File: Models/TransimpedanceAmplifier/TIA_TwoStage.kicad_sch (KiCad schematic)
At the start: 8 parts

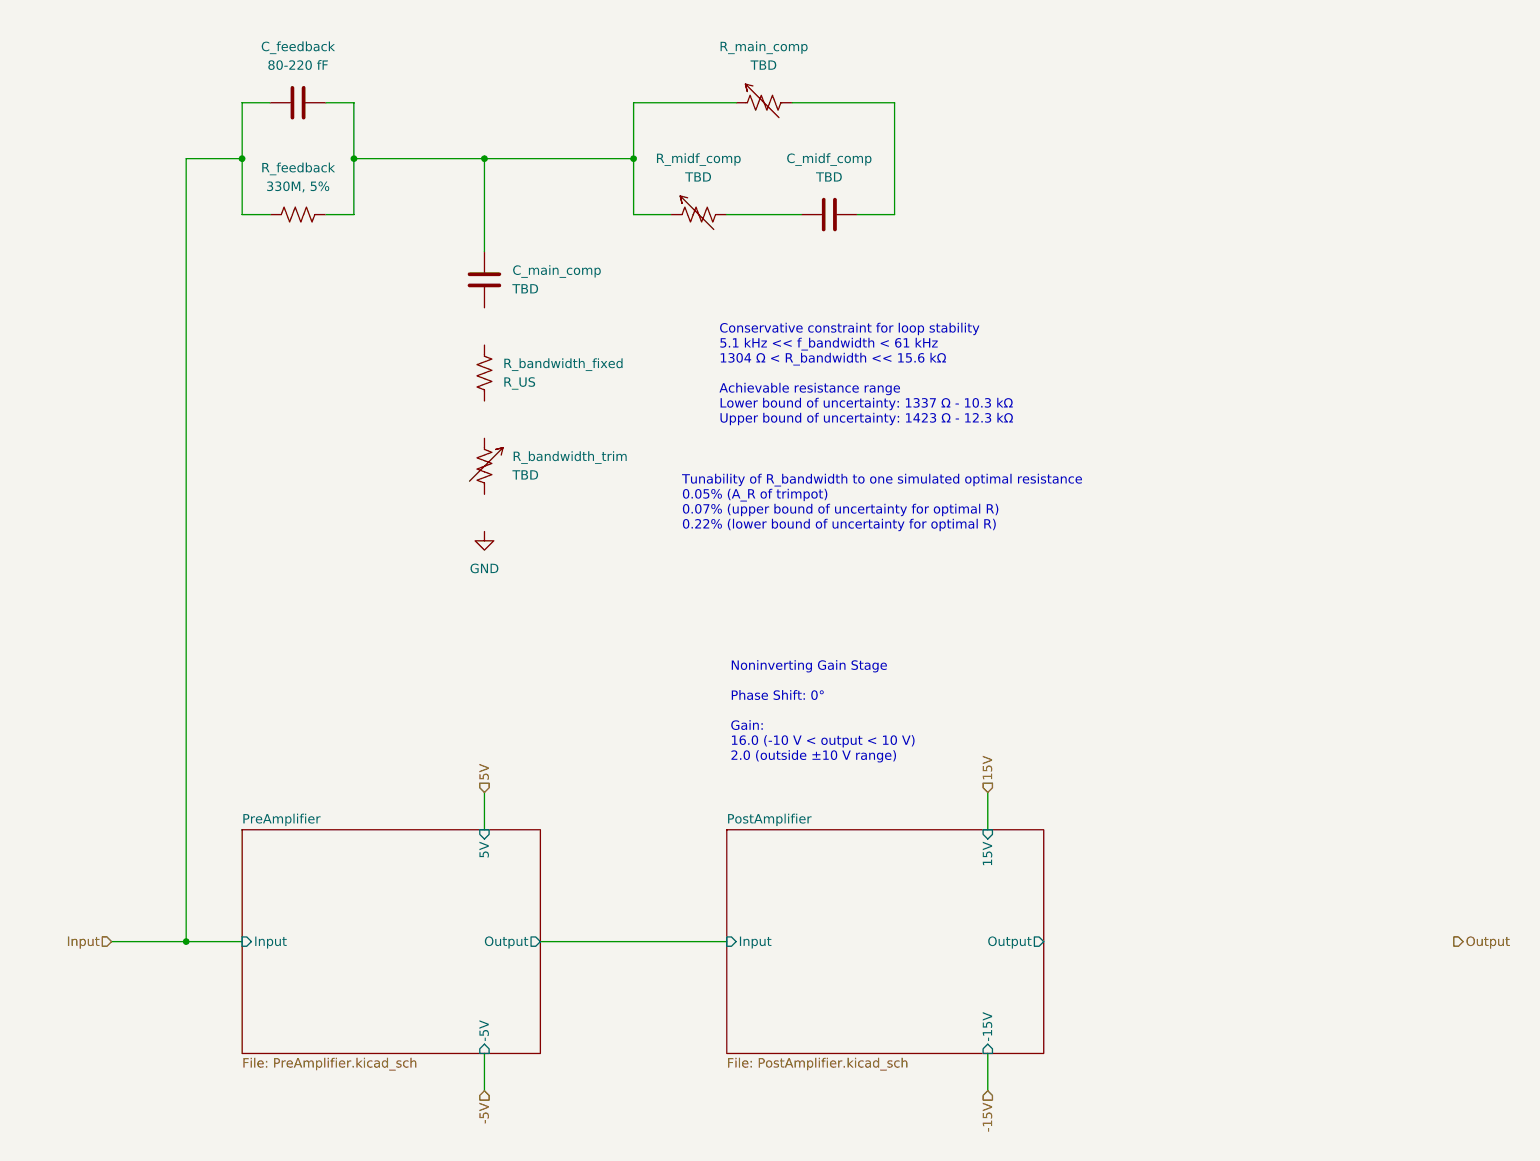
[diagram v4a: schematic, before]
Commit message: Figured out the specific part values for the pole-zero compensation network
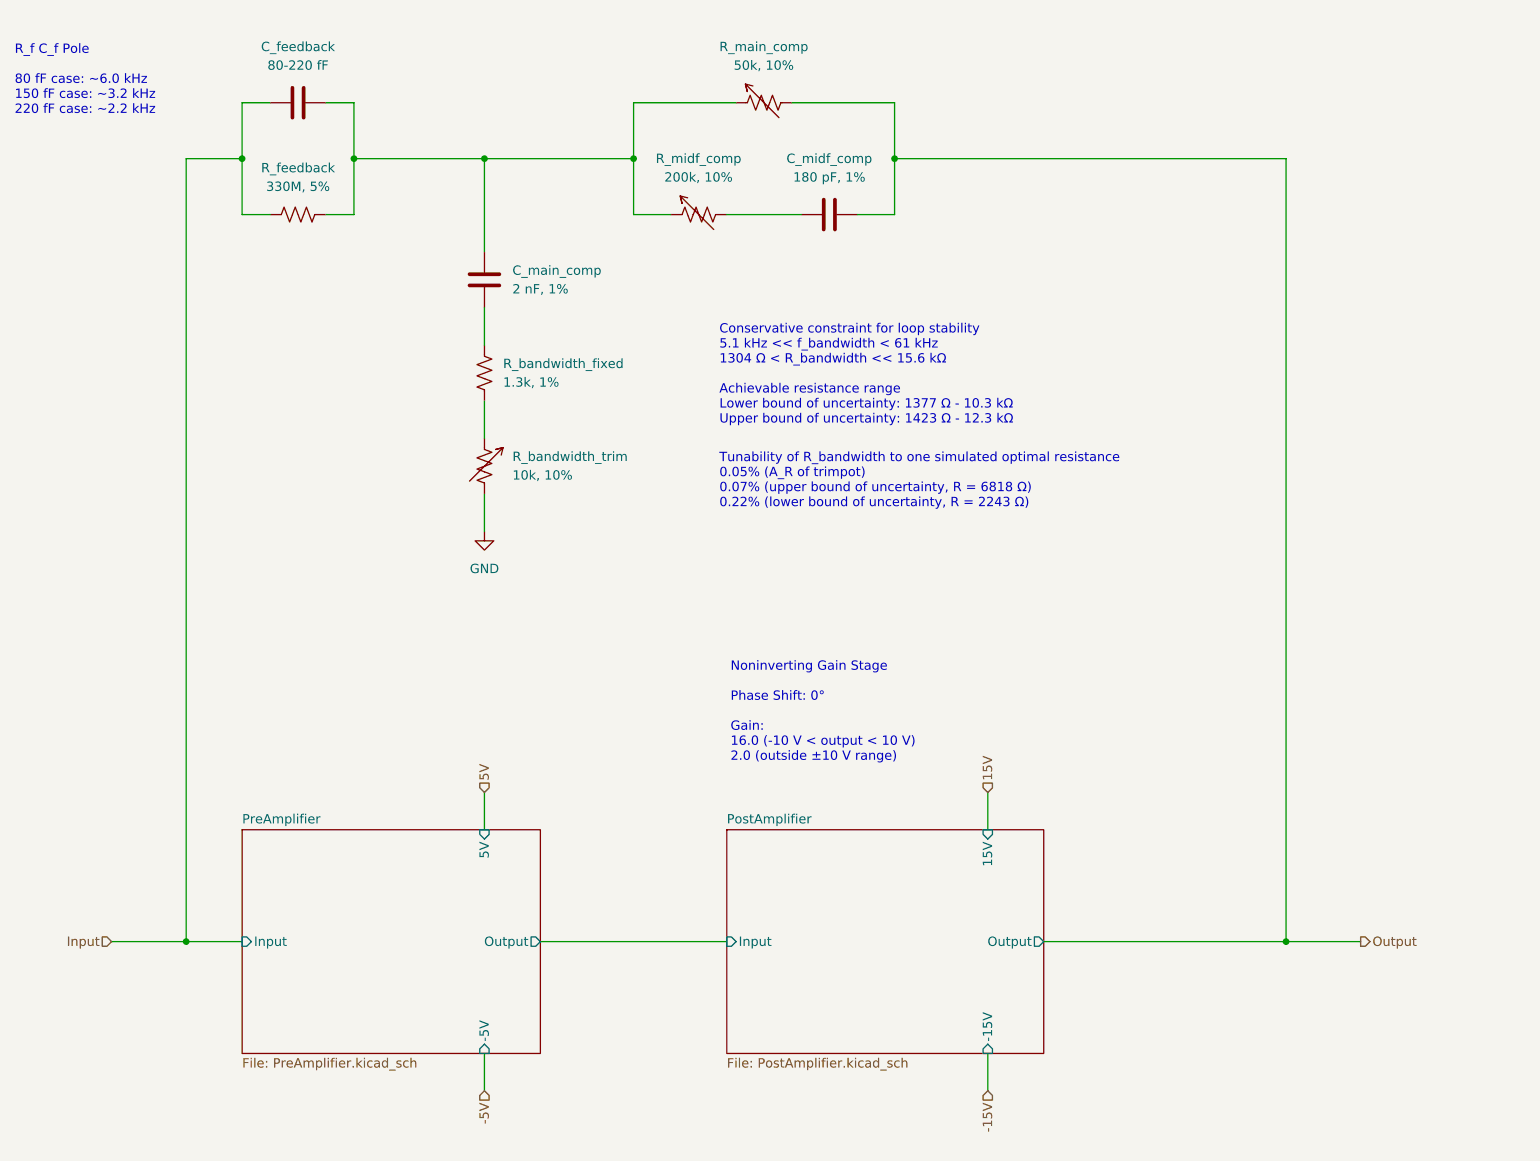
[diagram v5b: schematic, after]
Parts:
- C_main_comp: value TBD -> 2 nF, 1%; Purchase Link (none) -> https://www.digikey.com/en/products/detail/murata-electroni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
- C_midf_comp: value TBD -> 180 pF, 1%; Purchase Link (none) -> https://www.digikey.com/en/products/detail/murata-electroni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
- R_bandwidth_fixed: value R_US -> 1.3k, 1%; Purchase Link (none) -> https://www.digikey.com/en/products/detail/vishay-dale/CRCW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
- R_bandwidth_trim: value TBD -> 10k, 10%
- R_main_comp: value TBD -> 50k, 10%
- R_midf_comp: value TBD -> 200k, 10%
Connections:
- net GND: now also R_bandwidth_trim.2
- net Output: now also C_midf_comp.2, R_main_comp.2
- net at C_main_comp.2: now also R_bandwidth_fixed.1
- net at R_bandwidth_fixed.2: now also R_bandwidth_trim.1
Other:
- note added: "Conservative constraint for loop stability 5.1 kHz << f_bandwidth < 61 kHz 1304 Ω < R_bandwidth << 15.6 kΩ Achievable resistance range Lower bound of uncertainty: 1377 Ω - 10.3 kΩ Upper bound of uncertainty: 1423 Ω - 12.3 kΩ"
- note added: "R_f C_f Pole 80 fF case: ~6.0 kHz 150 fF case: ~3.2 kHz 220 fF case: ~2.2 kHz"
- note added: "Tunability of R_bandwidth to one simulated optimal resistance 0.05% (A_R of trimpot) 0.07% (upper bound of uncertainty, R = 6818 Ω) 0.22% (lower bound of uncertainty, R = 2243 Ω)"
- note removed: "Conservative constraint for loop stability 5.1 kHz << f_bandwidth < 61 kHz 1304 Ω < R_bandwidth << 15.6 kΩ Achievable resistance range Lower bound of uncertainty: 1337 Ω - 10.3 kΩ Upper bound of uncertainty: 1423 Ω - 12.3 kΩ"
- note removed: "Tunability of R_bandwidth to one simulated optimal resistance 0.05% (A_R of trimpot) 0.07% (upper bound of uncertainty for optimal R) 0.22% (lower bound of uncertainty for optimal R)"
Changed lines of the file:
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@@
 	(generator_version "9.0")
 	(paper "A4")
-	(text "Conservative constraint for loop stability\n5.1 kHz << f_bandwidth < 61 kHz\n1304 Ω < R_bandwidth << 15.6 kΩ\n\nAchievable resistance range\nLower bound of uncertainty: 1337 Ω - 10.3 kΩ\nUpper bound of uncertainty: 1423 Ω - 12.3 kΩ"
+	(text "Conservative constraint for loop stability\n5.1 kHz << f_bandwidth < 61 kHz\n1304 Ω < R_bandwidth << 15.6 kΩ\n\nAchievable resistance range\nLower bound of uncertainty: 1377 Ω - 10.3 kΩ\nUpper bound of uncertainty: 1423 Ω - 12.3 kΩ"
 		(exclude_from_sim no)
 		(at 125.984 63.246 0)
@@
 		)
 	)
-	(text "Tunability of R_bandwidth to one simulated optimal resistance\n0.05% (A_R of trimpot)\n0.07% (upper bound of uncertainty for optimal R)\n0.22% (lower bound of uncertainty for optimal R)"
-		(exclude_from_sim no)
-		(at 120.904 83.82 0)
+	(text "Tunability of R_bandwidth to one simulated optimal resistance\n0.05% (A_R of trimpot)\n0.07% (upper bound of uncertainty, R = 6818 Ω)\n0.22% (lower bound of uncertainty, R = 2243 Ω)"
+		(exclude_from_sim no)
+		(at 125.984 80.772 0)
+		(effects
+			(font
+				(size 1.27 1.27)
+			)
+			(justify left top)
+		)
+	)
+	(text "R_f C_f Pole\n\n80 fF case: ~6.0 kHz\n150 fF case: ~3.2 kHz\n220 fF case: ~2.2 kHz"
+		(exclude_from_sim no)
+		(at 29.972 25.146 0)
 		(effects
 			(font
@@
 	)
 	(junction
+		(at 149.86 40.64)
+		(diameter 0)
+		(color 0 0 0 0)
+	)
+	(junction
 		(at 60.96 40.64)
 		(diameter 0)
@@
 	)
 	(junction
+		(at 203.2 147.32)
+		(diameter 0)
+		(color 0 0 0 0)
+	)
+	(junction
 		(at 114.3 40.64)
 		(diameter 0)
@@
 	(wire
 		(pts
+			(xy 93.98 86.36) (xy 93.98 91.44)
+		)
+		(stroke
+			(width 0)
+			(type default)
+		)
+	)
+	(wire
+		(pts
 			(xy 76.2 40.64) (xy 93.98 40.64)
 		)
@@
 	(wire
 		(pts
+			(xy 149.86 40.64) (xy 203.2 40.64)
+		)
+		(stroke
+			(width 0)
+			(type default)
+		)
+	)
+	(wire
+		(pts
 			(xy 93.98 162.56) (xy 93.98 167.64)
 		)
@@
 	(wire
 		(pts
-			(xy 149.86 33.02) (xy 149.86 48.26)
+			(xy 170.18 147.32) (xy 203.2 147.32)
+		)
+		(stroke
+			(width 0)
+			(type default)
+		)
+	)
+	(wire
+		(pts
+			(xy 149.86 33.02) (xy 149.86 40.64)
 		)
 		(stroke
@@
 	(wire
 		(pts
+			(xy 203.2 147.32) (xy 213.36 147.32)
+		)
+		(stroke
+			(width 0)
+			(type default)
+		)
+	)
+	(wire
+		(pts
+			(xy 93.98 60.96) (xy 93.98 66.04)
+		)
+		(stroke
+			(width 0)
+			(type default)
+		)
+	)
+	(wire
+		(pts
 			(xy 53.34 147.32) (xy 60.96 147.32)
 		)
@@
 	(wire
 		(pts
+			(xy 149.86 40.64) (xy 149.86 48.26)
+		)
+		(stroke
+			(width 0)
+			(type default)
+		)
+	)
+	(wire
+		(pts
 			(xy 60.96 40.64) (xy 53.34 40.64)
+		)
+		(stroke
+			(width 0)
+			(type default)
+		)
+	)
+	(wire
+		(pts
+			(xy 203.2 40.64) (xy 203.2 147.32)
+		)
+		(stroke
+			(width 0)
+			(type default)
+		)
+	)
+	(wire
+		(pts
+			(xy 93.98 73.66) (xy 93.98 78.74)
 		)
 		(stroke
@@
 	(hierarchical_label "Output"
 		(shape output)
-		(at 226.06 147.32 0)
+		(at 213.36 147.32 0)
 		(effects
 			(font
@@
 			)
 		)
-		(property "Value" "TBD"
+		(property "Value" "2 nF, 1%"
 			(at 97.79 58.4199 0)
 			(effects
@@
 		)
 		(property "Description" "Unpolarized capacitor"
+			(at 93.98 57.15 0)
+			(effects
+				(font
+					(size 1.27 1.27)
+				)
+				(hide yes)
+			)
+		)
+		(property "Purchase Link" "https://www.digikey.com/en/products/detail/murata-electronics/GCM1885C1H202FA16D/16033535"
 			(at 93.98 57.15 0)
 			(effects
@@
 			)
 		)
-		(property "Value" "R_US"
+		(property "Value" "1.3k, 1%"
 			(at 96.52 71.1199 0)
 			(effects
@@
 		)
 		(property "Description" "Resistor, US symbol"
+			(at 93.98 69.85 0)
+			(effects
+				(font
+					(size 1.27 1.27)
+				)
+				(hide yes)
+			)
+		)
+		(property "Purchase Link" "https://www.digikey.com/en/products/detail/vishay-dale/CRCW06031K30FKEA/1174680"
 			(at 93.98 69.85 0)
 			(effects
@@
 			)
 		)
-		(property "Value" "TBD"
+		(property "Value" "50k, 10%"
 			(at 132.0419 27.94 90)
 			(effects
@@
 			)
 		)
-		(property "Value" "TBD"
+		(property "Value" "200k, 10%"
 			(at 123.1519 43.18 90)
 			(effects
@@
 			)
 		)
-		(property "Value" "TBD"
+		(property "Value" "180 pF, 1%"
 			(at 140.97 43.18 90)
 			(effects
@@
 		)
 		(property "Description" "Unpolarized capacitor"
+			(at 140.97 48.26 0)
+			(effects
+				(font
+					(size 1.27 1.27)
+				)
+				(hide yes)
+			)
+		)
+		(property "Purchase Link" "https://www.digikey.com/en/products/detail/murata-electronics/GCM1885C2A181FA16D/7363158"
 			(at 140.97 48.26 0)
 			(effects
@@
 			)
 		)
-		(property "Value" "TBD"
+		(property "Value" "10k, 10%"
 			(at 97.79 83.7818 0)
 			(effects

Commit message: Finalized all trimpot models
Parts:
- R_bandwidth_trim, R_main_comp, R_midf_comp: Purchase Link (none) -> https://www.digikey.com/en/products/detail/bourns-inc/3269W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
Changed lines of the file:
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@@
+			)
+		)
+		(property "Purchase Link" "https://www.digikey.com/en/products/detail/bourns-inc/3269W-1-503GLF/2535614"
+			(at 132.08 33.02 0)
+			(effects
+				(font
+					(size 1.27 1.27)
+				)
+				(hide yes)
 			)
 		)
@@
 			)
 		)
+		(property "Purchase Link" "https://www.digikey.com/en/products/detail/bourns-inc/3269W-1-204GLF/2535590"
+			(at 123.19 48.26 0)
+			(effects
+				(font
+					(size 1.27 1.27)
+				)
+				(hide yes)
+			)
+		)
 		(pin "1"
 		)
@@
 			(at 93.98 82.55 0)
 			(effects
+				(font
+					(size 1.27 1.27)
+				)
+				(hide yes)
+			)
+		)
+		(property "Purchase Link" "https://www.digikey.com/en/products/detail/bourns-inc/3269W-1-103GLF/2535568"
+			(at 93.98 82.55 0)
+			(effects

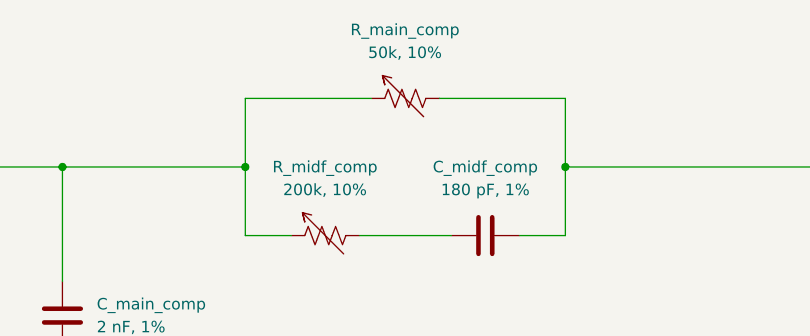
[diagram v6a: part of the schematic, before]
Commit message: Overhauled the purchase links for regulators and trimpots
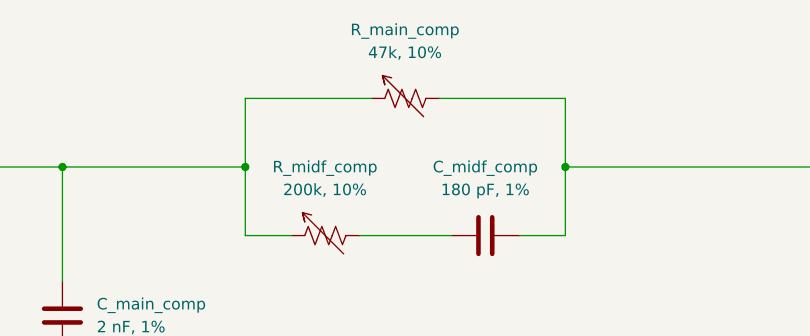
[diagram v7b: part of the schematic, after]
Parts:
- R_bandwidth_trim, R_midf_comp: Purchase Link https://www.digikey.com/en/products/detail/bourns-inc/3269W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 -> https://www.digikey.com/en/products/detail/bourns-inc/3296Y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
- R_main_comp: value 50k, 10% -> 47k, 10%; Purchase Link https://www.digikey.com/en/products/detail/bourns-inc/3269W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 -> https://www.digikey.com/en/products/detail/bourns-inc/3296Y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
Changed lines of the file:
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@@
 			)
 		)
-		(property "Value" "50k, 10%"
+		(property "Value" "47k, 10%"
 			(at 132.0419 27.94 90)
 			(effects
@@
 			)
 		)
-		(property "Purchase Link" "https://www.digikey.com/en/products/detail/bourns-inc/3269W-1-503GLF/2535614"
+		(property "Purchase Link" "https://www.digikey.com/en/products/detail/bourns-inc/3296Y-1-473LF/2536018"
 			(at 132.08 33.02 0)
 			(effects
@@
 			)
 		)
-		(property "Purchase Link" "https://www.digikey.com/en/products/detail/bourns-inc/3269W-1-204GLF/2535590"
+		(property "Purchase Link" "https://www.digikey.com/en/products/detail/bourns-inc/3296Y-1-204LF/1088092"
 			(at 123.19 48.26 0)
 			(effects
@@
 			)
 		)
-		(property "Purchase Link" "https://www.digikey.com/en/products/detail/bourns-inc/3269W-1-103GLF/2535568"
+		(property "Purchase Link" "https://www.digikey.com/en/products/detail/bourns-inc/3296Y-1-103LF/1088085"
 			(at 93.98 82.55 0)
 			(effects

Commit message: Refactoring in progress
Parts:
- C_feedback: now left out of the parts list
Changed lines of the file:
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@@
 		(unit 1)
 		(exclude_from_sim no)
-		(in_bom yes)
+		(in_bom no)
 		(on_board no)
 		(dnp no)
